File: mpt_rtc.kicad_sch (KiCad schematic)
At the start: 1 part

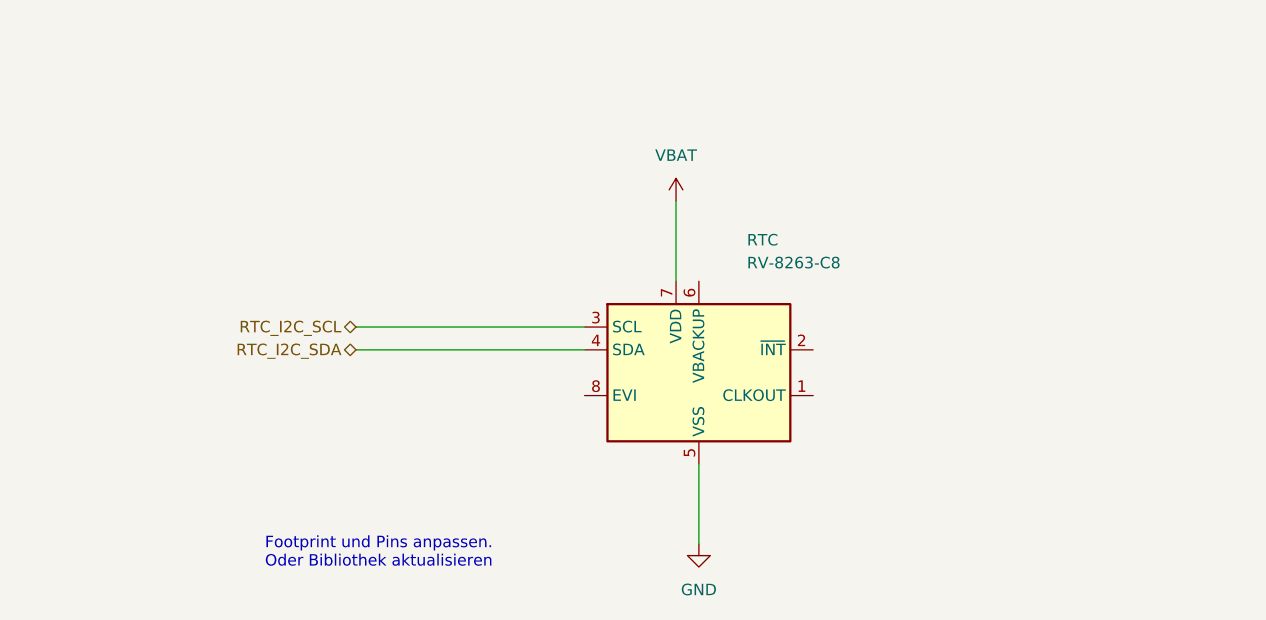
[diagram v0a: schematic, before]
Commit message: RTC Finished, changes to User Buttons
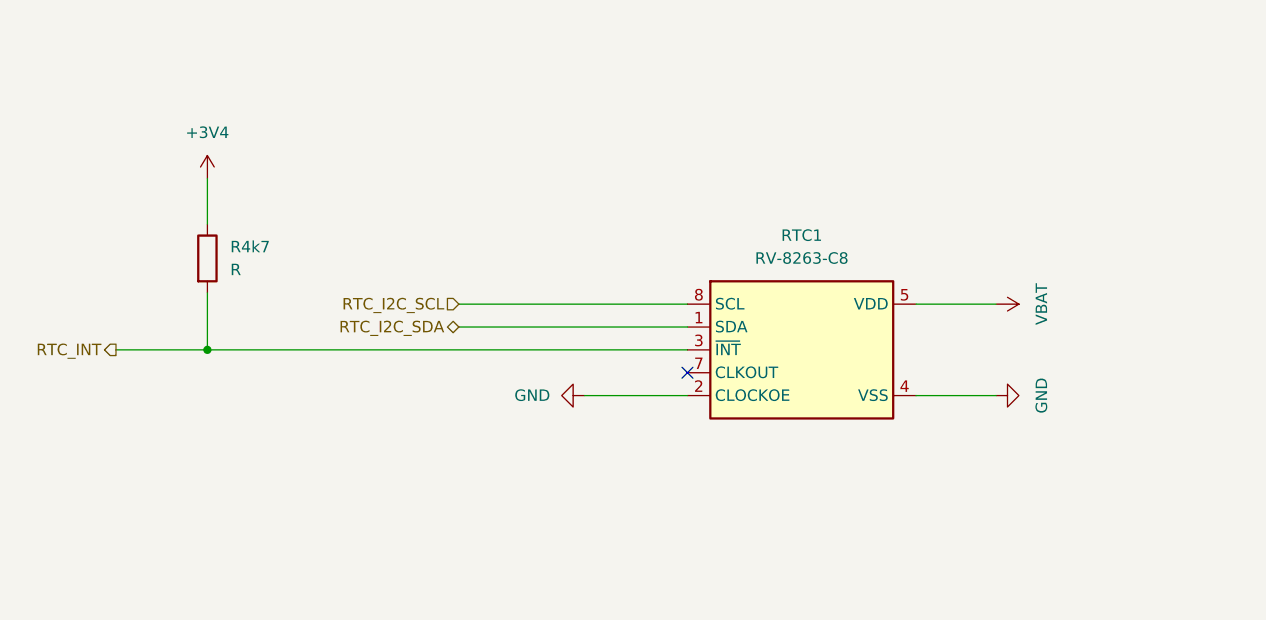
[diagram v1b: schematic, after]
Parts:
- removed RTC: RV-8263-C8, symbol Timer_RTC:RV-3028-C7
- added R4k7: R, symbol Device:R
- added RTC1: RV-8263-C8, Package_SON:MicroCrystal_C7_SON-8_1.5x3.2mm_P0.9mm, symbol MPT_Library:RV-8263-C8
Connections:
- net GND: now also RTC1.2 (CLOCKOE), RTC1.4 (VSS)
- net RTC_I2C_SCL: now also RTC1.8 (SCL)
- net RTC_I2C_SDA: now also RTC1.1 (SDA)
- net VBAT: now also RTC1.5 (VDD)
- new net +3V4: R4k7.1
- new net RTC_INT: R4k7.2, RTC1.3 (~{INT})
- no-connect marks 0 -> 1
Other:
- note removed: "Footprint und Pins anpassen. Oder Bibliothek aktualisieren"

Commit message: Footprints and Symbols for SW, RTC and Joystick
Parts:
- RTC1: footprint Package_SON:MicroCrystal_C7_SON-8_1.5x3.2mm_P0.9mm -> RV_8263_C8_32_768KHZ_20PPM_TA_QC:IC_RV-8263-C8-32.768KHZ-20PPM-TA-QC
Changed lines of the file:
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@@
 			)
 		)
-		(property "Footprint" "Package_SON:MicroCrystal_C7_SON-8_1.5x3.2mm_P0.9mm"
+		(property "Footprint" "RV_8263_C8_32_768KHZ_20PPM_TA_QC:IC_RV-8263-C8-32.768KHZ-20PPM-TA-QC"
 			(at 173.736 127.508 0)
 			(hide yes)

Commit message: RTC and User Buttons small changes
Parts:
- added C23: 100nF, symbol Device:C
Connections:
- net GND: now also C23.2
- net VBAT: now also C23.1
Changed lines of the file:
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@@
+		(color 0 0 0 0)
+	)
+	(junction
+		(at 161.29 123.19)
+		(diameter 0)
+		(color 0 0 0 0)
+	)
+	(junction
+		(at 161.29 113.03)
+		(diameter 0)
 		(color 0 0 0 0)
 	)
@@
 	(wire
 		(pts
-			(xy 114.3 123.19) (xy 125.73 123.19)
+			(xy 119.38 123.19) (xy 125.73 123.19)
+		)
+		(stroke
+			(width 0)
+			(type default)
+		)
+	)
+	(wire
+		(pts
+			(xy 161.29 123.19) (xy 161.29 121.92)
+		)
+		(stroke
+			(width 0)
+			(type default)
+		)
+	)
+	(wire
+		(pts
+			(xy 151.13 123.19) (xy 161.29 123.19)
+		)
+		(stroke
+			(width 0)
+			(type default)
+		)
+	)
+	(wire
+		(pts
+			(xy 119.38 130.81) (xy 119.38 123.19)
 		)
 		(stroke
@@
 	(wire
 		(pts
-			(xy 160.02 113.03) (xy 151.13 113.03)
-		)
-		(stroke
-			(width 0)
-			(type default)
-		)
-	)
-	(wire
-		(pts
-			(xy 151.13 123.19) (xy 160.02 123.19)
+			(xy 161.29 123.19) (xy 161.29 130.81)
+		)
+		(stroke
+			(width 0)
+			(type default)
+		)
+	)
+	(wire
+		(pts
+			(xy 161.29 104.14) (xy 161.29 113.03)
 		)
 		(stroke
@@
 	(wire
 		(pts
+			(xy 161.29 113.03) (xy 161.29 114.3)
+		)
+		(stroke
+			(width 0)
+			(type default)
+		)
+	)
+	(wire
+		(pts
 			(xy 100.33 115.57) (xy 125.73 115.57)
 		)
@@
 		(pts
 			(xy 62.23 118.11) (xy 72.39 118.11)
+		)
+		(stroke
+			(width 0)
+			(type default)
+		)
+	)
+	(wire
+		(pts
+			(xy 161.29 113.03) (xy 151.13 113.03)
 		)
 		(stroke
@@
 			)
 			(justify right)
+		)
+	)
+	(symbol
+		(lib_id "Device:C")
+		(at 161.29 118.11 0)
+		(unit 1)
+		(body_style 1)
+		(exclude_from_sim no)
+		(in_bom yes)
+		(on_board yes)
+		(in_pos_files yes)
+		(dnp no)
+		(fields_autoplaced yes)
+		(property "Reference" "C23"
+			(at 165.1 116.8399 0)
+			(show_name no)
+			(do_not_autoplace no)
+			(effects
+				(font
+					(size 1.27 1.27)
+				)
+				(justify left)
+			)
+		)
+		(property "Value" "100nF"
+			(at 165.1 119.3799 0)
+			(show_name no)
+			(do_not_autoplace no)
+			(effects
+				(font
+					(size 1.27 1.27)
+				)
+				(justify left)
+			)
+		)
+		(property "Footprint" ""
+			(at 162.2552 121.92 0)
+			(hide yes)
+			(show_name no)
+			(do_not_autoplace no)
+			(effects
+				(font
+					(size 1.27 1.27)
+				)
+			)
+		)
+		(property "Datasheet" ""
+			(at 161.29 118.11 0)
+			(hide yes)
+			(show_name no)
+			(do_not_autoplace no)
+			(effects
+				(font
+					(size 1.27 1.27)
+				)
+			)
+		)
+		(property "Description" "Unpolarized capacitor"
+			(at 161.29 118.11 0)
+			(hide yes)
+			(show_name no)
+			(do_not_autoplace no)
+			(effects
+				(font
+					(size 1.27 1.27)
+				)
+			)
+		)
+		(pin "2"
+		)
+		(pin "1"
+		)
+		(instances
+			(project "MPT"
+				(path "/328ebaa0-d01b-4b80-b614-bb0154e8d306/29fc7d94-8fee-43e7-bab5-72b4e39e651f"
+					(reference "C23")
+					(unit 1)
+				)
+			)
 		)
 	)
@@
 	(symbol
 		(lib_id "power:GND")
-		(at 114.3 123.19 270)
+		(at 119.38 130.81 0)
 		(unit 1)
 		(body_style 1)
@@
 		(fields_autoplaced yes)
 		(property "Reference" "#PWR045"
-			(at 107.95 123.19 0)
+			(at 119.38 137.16 0)
 			(hide yes)
 			(show_name no)
@@
 		)
 		(property "Value" "GND"
-			(at 110.49 123.1899 90)
-			(show_name no)
-			(do_not_autoplace no)
-			(effects
-				(font
-					(size 1.27 1.27)
-				)
-				(justify right)
+			(at 121.92 132.0799 0)
+			(show_name no)
+			(do_not_autoplace no)
+			(effects
+				(font
+					(size 1.27 1.27)
+				)
+				(justify left)
 			)
 		)
 		(property "Footprint" ""
-			(at 114.3 123.19 0)
+			(at 119.38 130.81 0)
 			(hide yes)
 			(show_name no)
@@
 		)
 		(property "Datasheet" ""
-			(at 114.3 123.19 0)
+			(at 119.38 130.81 0)
 			(hide yes)
 			(show_name no)
@@
 		)
 		(property "Description" "Power symbol creates a global label with name \"GND\" , ground"
-			(at 114.3 123.19 0)
+			(at 119.38 130.81 0)
 			(hide yes)
 			(show_name no)
@@
 	(symbol
 		(lib_id "power:VAA")
-		(at 160.02 113.03 270)
+		(at 161.29 104.14 0)
 		(unit 1)
 		(body_style 1)
@@
 		(fields_autoplaced yes)
 		(property "Reference" "#PWR047"
-			(at 156.21 113.03 0)
+			(at 161.29 107.95 0)
 			(hide yes)
 			(show_name no)
@@
 		)
 		(property "Value" "VBAT"
-			(at 165.1 113.03 0)
-			(show_name no)
-			(do_not_autoplace no)
-			(effects
-				(font
-					(size 1.27 1.27)
-				)
+			(at 163.83 102.8699 0)
+			(show_name no)
+			(do_not_autoplace no)
+			(effects
+				(font
+					(size 1.27 1.27)
+				)
+				(justify left)
 			)
 		)
 		(property "Footprint" ""
-			(at 160.02 113.03 0)
+			(at 161.29 104.14 0)
 			(hide yes)
 			(show_name no)
@@
 		)
 		(property "Datasheet" ""
-			(at 160.02 113.03 0)
+			(at 161.29 104.14 0)
 			(hide yes)
 			(show_name no)
@@
 		)
 		(property "Description" "Power symbol creates a global label with name \"VAA\""
-			(at 160.02 113.03 0)
+			(at 161.29 104.14 0)
 			(hide yes)
 			(show_name no)
@@
 	(symbol
 		(lib_id "power:GND")
-		(at 160.02 123.19 90)
+		(at 161.29 130.81 0)
 		(unit 1)
 		(body_style 1)
@@
 		(fields_autoplaced yes)
 		(property "Reference" "#PWR048"
-			(at 166.37 123.19 0)
+			(at 161.29 137.16 0)
 			(hide yes)
 			(show_name no)
@@
 		)
 		(property "Value" "GND"
-			(at 165.1 123.19 0)
-			(show_name no)
-			(do_not_autoplace no)
-			(effects
-				(font
-					(size 1.27 1.27)
-				)
+			(at 163.83 132.0799 0)
+			(show_name no)
+			(do_not_autoplace no)
+			(effects
+				(font
+					(size 1.27 1.27)
+				)
+				(justify left)
 			)
 		)
 		(property "Footprint" ""
-			(at 160.02 123.19 0)
+			(at 161.29 130.81 0)
 			(hide yes)
 			(show_name no)
@@
 		)
 		(property "Datasheet" ""
-			(at 160.02 123.19 0)
+			(at 161.29 130.81 0)
 			(hide yes)
 			(show_name no)
@@
 		)
 		(property "Description" "Power symbol creates a global label with name \"GND\" , ground"
-			(at 160.02 123.19 0)
-			(hide yes)
-			(show_name no)
+			(at 161.29 130.81 0)
+			(hide yes)
+			(show_name no)

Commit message: Sleep Control Sub-Sheet created, Hirarchy Labels renamed connected
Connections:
- net RTC_I2C_SCL renamed I2C_SCL
- net RTC_I2C_SDA renamed I2C_SDA
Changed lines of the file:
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@@
 		)
 	)
-	(hierarchical_label "RTC_I2C_SCL"
+	(hierarchical_label "I2C_SCL"
 		(shape input)
 		(at 100.33 113.03 180)
@@
 		)
 	)
-	(hierarchical_label "RTC_I2C_SDA"
+	(hierarchical_label "I2C_SDA"
 		(shape bidirectional)
 		(at 100.33 115.57 180)

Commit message: Make Block Titles consistent in size Remove not connected marks on mcu for pins which can be used for user buttons and other stuff Add User button hierarchy lables for Button 4 & 5 on MCU sheet Fix hierarchichal pin names on the block not matching the sheet
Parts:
- removed C23: 100nF, symbol Device:C
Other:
- moved on the sheet: R4k7, RTC1

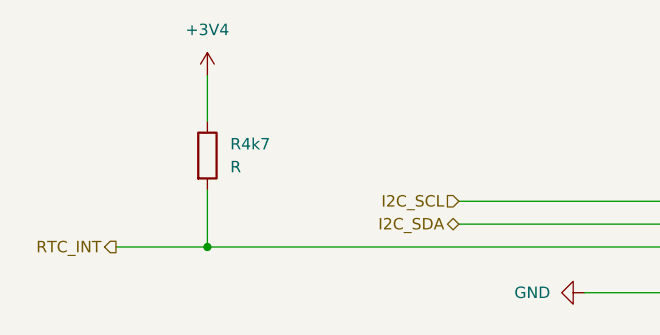
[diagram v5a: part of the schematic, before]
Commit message: Footprints added, Userbuttons and RTC added on PCB Layout
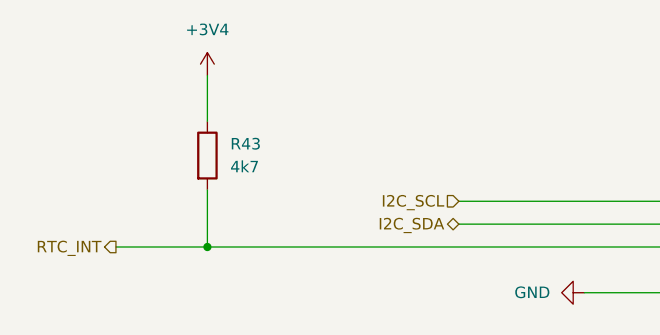
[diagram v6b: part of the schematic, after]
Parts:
- removed R4k7: R, symbol Device:R
- added R43: 4k7, Resistor_SMD:R_0603_1608Metric, symbol Device:R
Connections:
- net +3V4: now also R43.1
- net RTC_INT: now also R43.2
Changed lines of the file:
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@@
+	)
+	(symbol
+		(lib_id "Device:R")
+		(at 93.98 96.52 0)
+		(unit 1)
+		(body_style 1)
+		(exclude_from_sim no)
+		(in_bom yes)
+		(on_board yes)
+		(in_pos_files yes)
+		(dnp no)
+		(fields_autoplaced yes)
+		(property "Reference" "R43"
+			(at 96.52 95.2499 0)
+			(show_name no)
+			(do_not_autoplace no)
+			(effects
+				(font
+					(size 1.27 1.27)
+				)
+				(justify left)
+			)
+		)
+		(property "Value" "4k7"
+			(at 96.52 97.7899 0)
+			(show_name no)
+			(do_not_autoplace no)
+			(effects
+				(font
+					(size 1.27 1.27)
+				)
+				(justify left)
+			)
+		)
+		(property "Footprint" "Resistor_SMD:R_0603_1608Metric"
+			(at 92.202 96.52 90)
+			(hide yes)
+			(show_name no)
+			(do_not_autoplace no)
+			(effects
+				(font
+					(size 1.27 1.27)
+				)
+			)
+		)
+		(property "Datasheet" ""
+			(at 93.98 96.52 0)
+			(hide yes)
+			(show_name no)
+			(do_not_autoplace no)
+			(effects
+				(font
+					(size 1.27 1.27)
+				)
+			)
+		)
+		(property "Description" "Resistor"
+			(at 93.98 96.52 0)
+			(hide yes)
+			(show_name no)
+			(do_not_autoplace no)
+			(effects
+				(font
+					(size 1.27 1.27)
+				)
+			)
+		)
+		(pin "2"
+		)
+		(pin "1"
+		)
+		(instances
+			(project "MPT"
+				(path "/328ebaa0-d01b-4b80-b614-bb0154e8d306/29fc7d94-8fee-43e7-bab5-72b4e39e651f"
+					(reference "R43")
+					(unit 1)
+				)
+			)
+		)
 	)
 	(symbol
@@
 					(unit 1)
 				)
-			)
-		)
-	)
-	(symbol
-		(lib_id "Device:R")
-		(at 93.98 96.52 0)
-		(unit 1)
-		(body_style 1)
-		(exclude_from_sim no)
-		(in_bom yes)
-		(on_board yes)
-		(in_pos_files yes)
-		(dnp no)
-		(fields_autoplaced yes)
-		(property "Reference" "R4k7"
-			(at 96.52 95.2499 0)
-			(show_name no)
-			(do_not_autoplace no)
-			(effects
-				(font
-					(size 1.27 1.27)
-				)
-				(justify left)
-			)
-		)
-		(property "Value" "R"
-			(at 96.52 97.7899 0)
-			(show_name no)
-			(do_not_autoplace no)
-			(effects
-				(font
-					(size 1.27 1.27)
-				)
-				(justify left)
-			)
-		)
-		(property "Footprint" ""
-			(at 92.202 96.52 90)
-			(hide yes)
-			(show_name no)
-			(do_not_autoplace no)
-			(effects
-				(font
-					(size 1.27 1.27)
-				)
-			)
-		)
-		(property "Datasheet" ""
-			(at 93.98 96.52 0)
-			(hide yes)
-			(show_name no)
-			(do_not_autoplace no)
-			(effects
-				(font
-					(size 1.27 1.27)
-				)
-			)
-		)
-		(property "Description" "Resistor"
-			(at 93.98 96.52 0)
-			(hide yes)
-			(show_name no)
-			(do_not_autoplace no)
-			(effects
-				(font
-					(size 1.27 1.27)
-				)
-			)
-		)
-		(pin "2"
-		)
-		(pin "1"
-		)
-		(instances
-			(project "MPT"
-				(path "/328ebaa0-d01b-4b80-b614-bb0154e8d306/29fc7d94-8fee-43e7-bab5-72b4e39e651f"
-					(reference "R4k7")
-					(unit 1)
-				)
